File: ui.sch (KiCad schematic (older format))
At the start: 45 parts, among them SW1 SW_Push, SW2 SW_Push, SW3 SW_Push, SW4 SW_Push, SW5 SW_Push, SW8 JS202011SCQN, SW9 JS202011SCQN, U1 ICE40HX4K-TQ144

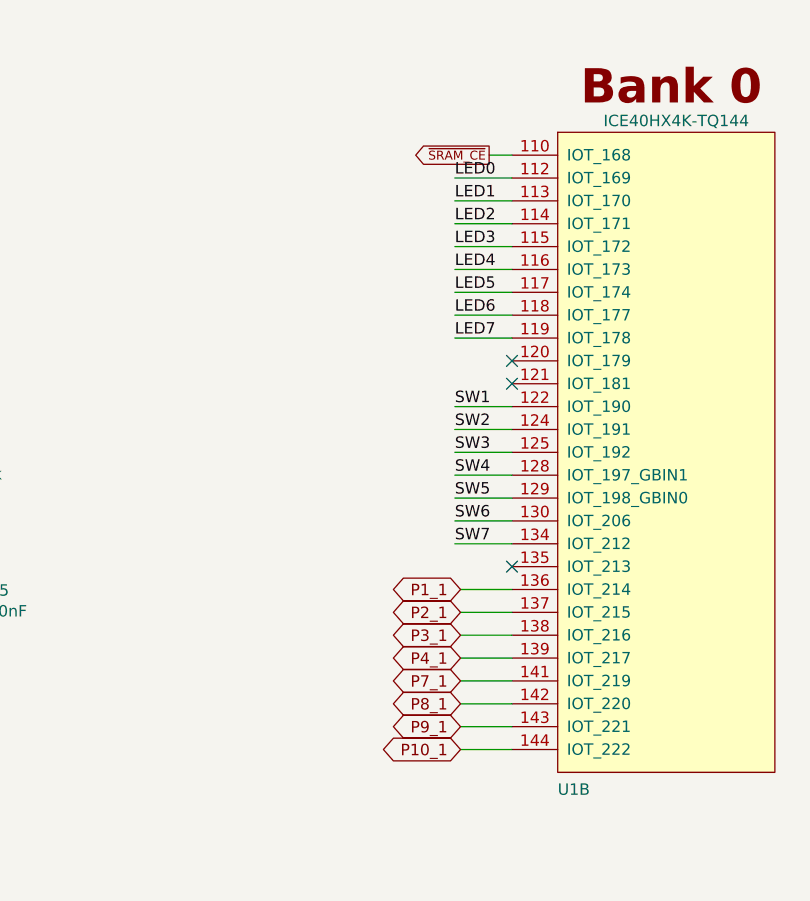
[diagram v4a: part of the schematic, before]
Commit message: Continued with routing and added ADC
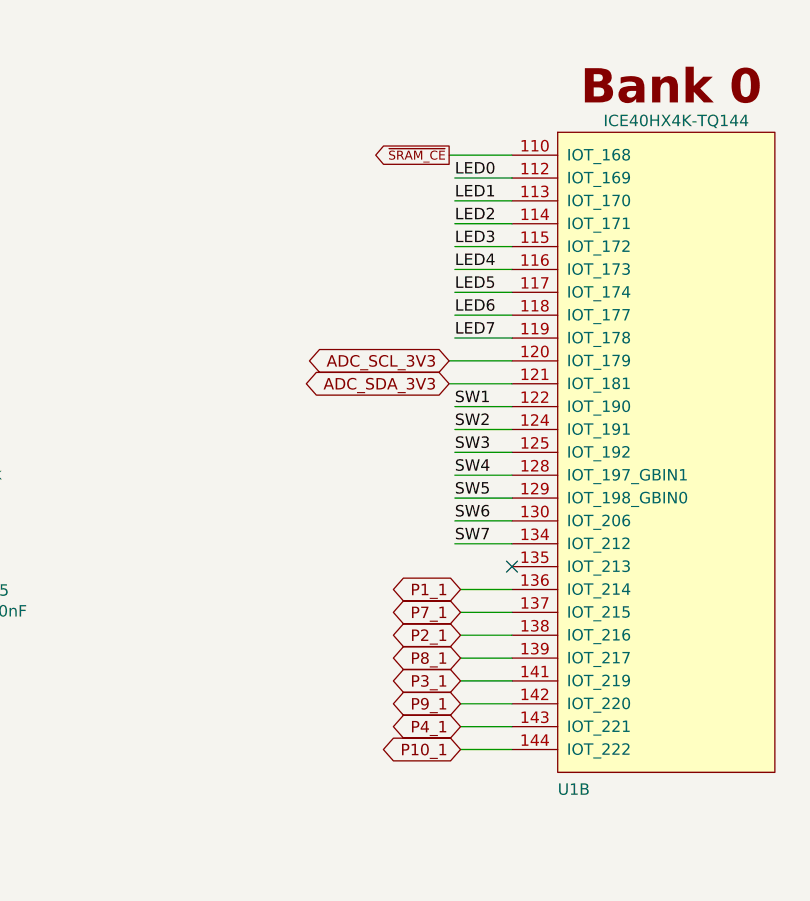
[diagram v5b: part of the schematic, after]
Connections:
- net P2_1: now also U1.138 (IOT_216); no longer U1.137 (IOT_215)
- net P3_1: now also U1.141 (IOT_219); no longer U1.138 (IOT_216)
- net P4_1: now also U1.143 (IOT_221); no longer U1.139 (IOT_217)
- net P7_1: now also U1.137 (IOT_215); no longer U1.141 (IOT_219)
- net P8_1: now also U1.139 (IOT_217); no longer U1.142 (IOT_220)
- net P9_1: now also U1.142 (IOT_220); no longer U1.143 (IOT_221)
- net ADC_SCL_3V3: now reaches U1.120 (IOT_179)
- net ADC_SDA_3V3: now reaches U1.121 (IOT_181)
- no-connect marks 11 -> 9
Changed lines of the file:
@@
 Text Label 8000 3150 0    50   ~ 0
 SW6
-Text GLabel 8025 4150 0    50   BiDi ~ 0
-P10_1
-Text GLabel 8025 4050 0    50   BiDi ~ 0
-P9_1
-Text GLabel 8025 3950 0    50   BiDi ~ 0
-P8_1
-Text GLabel 8025 3850 0    50   BiDi ~ 0
-P7_1
-Text GLabel 8025 3750 0    50   BiDi ~ 0
-P4_1
-Text GLabel 8025 3650 0    50   BiDi ~ 0
-P3_1
-Text GLabel 8025 3550 0    50   BiDi ~ 0
-P2_1
-Text GLabel 8025 3450 0    50   BiDi ~ 0
-P1_1
 Wire Wire Line
-	8025 4150 8250 4150
-Wire Wire Line
-	8025 4050 8250 4050
-Wire Wire Line
-	8025 3950 8250 3950
-Wire Wire Line
-	8025 3850 8250 3850
-Wire Wire Line
-	8025 3750 8250 3750
-Wire Wire Line
-	8025 3650 8250 3650
-Wire Wire Line
-	8025 3550 8250 3550
-Wire Wire Line
-	8025 3450 8250 3450
-Wire Wire Line
-	8150 1550 8250 1550
-Text GLabel 8150 1550 0    39   Output ~ 0
+	7975 1550 8250 1550
+Text GLabel 7975 1550 0    39   Output ~ 0
 ~SRAM_CE~
 Wire Wire Line
@@
 	1    0    0    -1
 $EndComp
-NoConn ~ 8250 2450
 NoConn ~ 8250 3350
-NoConn ~ 8250 2550
+Wire Wire Line
+	8025 3450 8250 3450
+Wire Wire Line
+	8025 3650 8250 3650
+Wire Wire Line
+	8025 3850 8250 3850
+Wire Wire Line
+	8025 4050 8250 4050
+Wire Wire Line
+	8025 3550 8250 3550
+Wire Wire Line
+	8025 3750 8250 3750
+Wire Wire Line
+	8025 3950 8250 3950
+Wire Wire Line
+	8025 4150 8250 4150
+Text GLabel 8025 3450 0    50   BiDi ~ 0
+P1_1
+Text GLabel 8025 3650 0    50   BiDi ~ 0
+P2_1
+Text GLabel 8025 3850 0    50   BiDi ~ 0
+P3_1
+Text GLabel 8025 4050 0    50   BiDi ~ 0
+P4_1
+Text GLabel 8025 3550 0    50   BiDi ~ 0
+P7_1
+Text GLabel 8025 3750 0    50   BiDi ~ 0
+P8_1
+Text GLabel 8025 3950 0    50   BiDi ~ 0
+P9_1
+Text GLabel 8025 4150 0    50   BiDi ~ 0
+P10_1
+Text GLabel 7975 2550 0    50   BiDi ~ 0
+ADC_SDA_3V3
+Text GLabel 7975 2450 0    50   BiDi ~ 0
+ADC_SCL_3V3
+Wire Wire Line
+	7975 2450 8250 2450
+Wire Wire Line
+	7975 2550 8250 2550
 $EndSCHEMATC

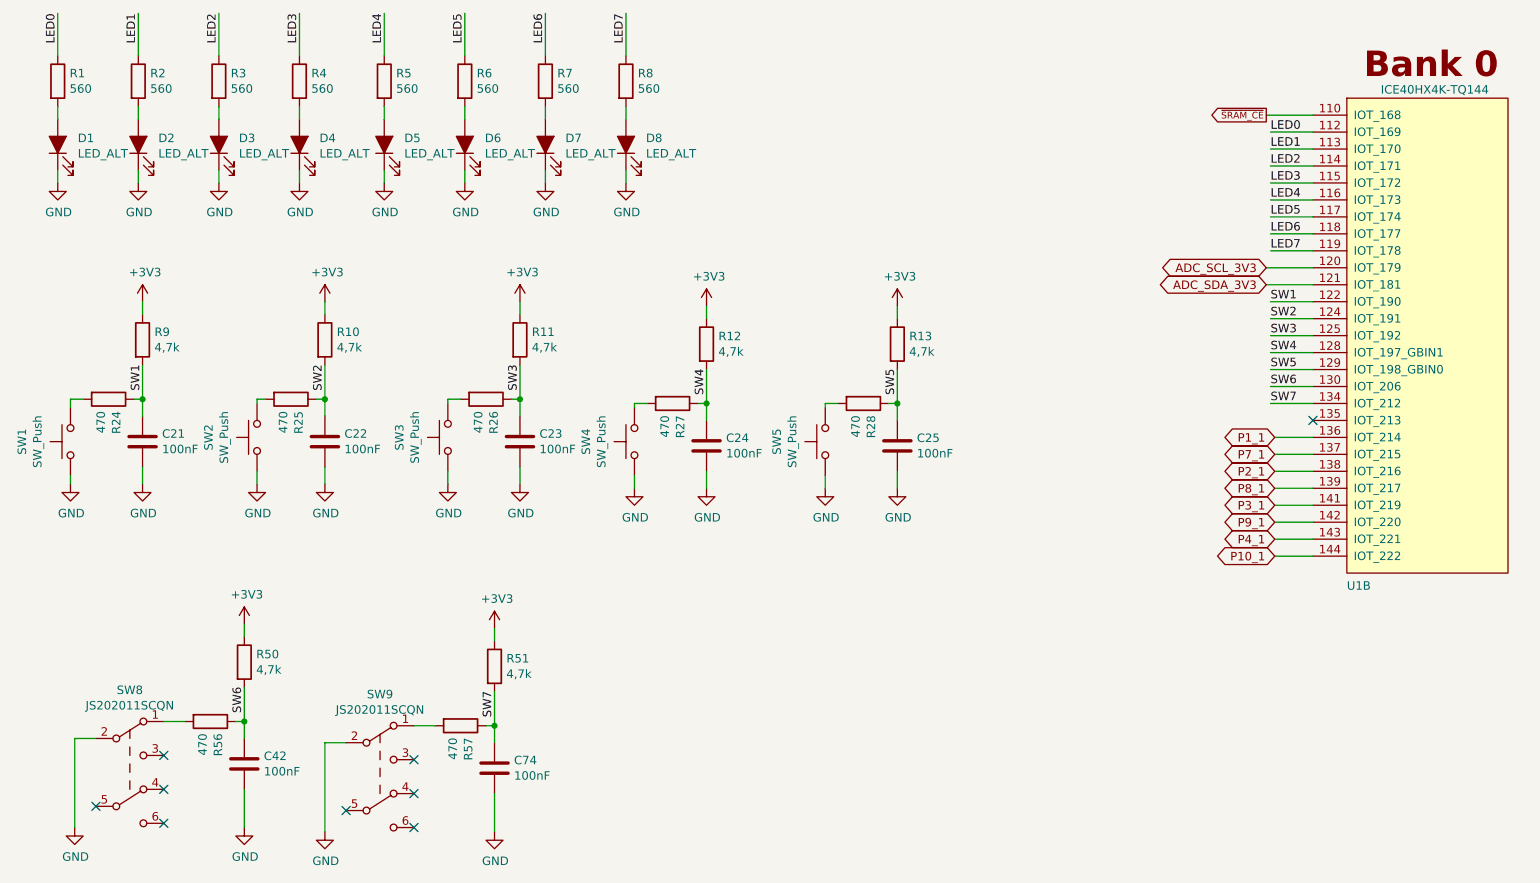
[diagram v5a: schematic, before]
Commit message: Added more BOM information, updated fpga symbol, added some more 3d models
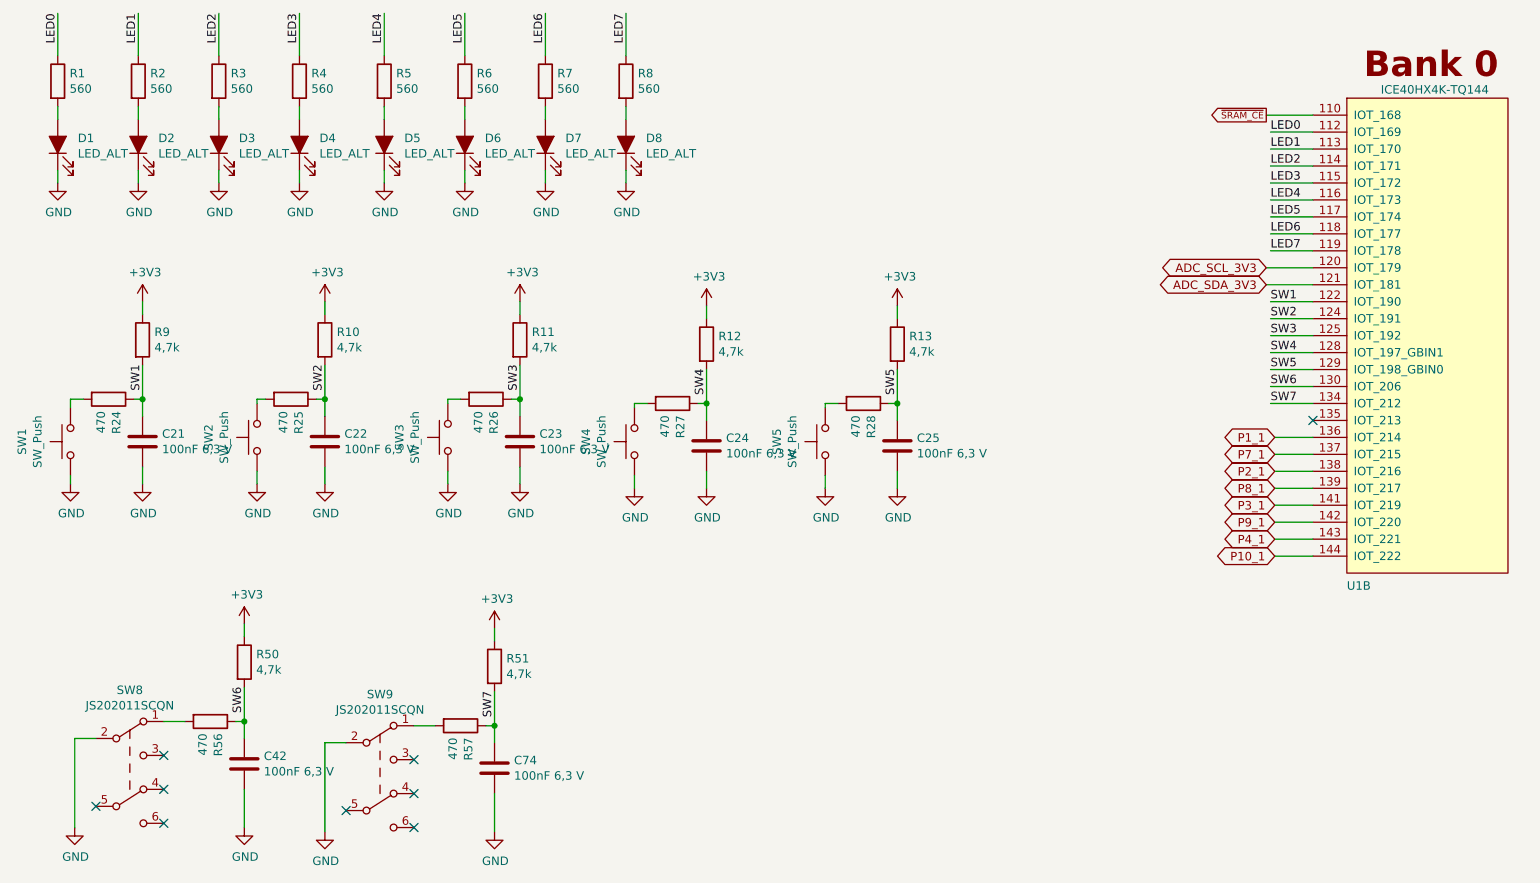
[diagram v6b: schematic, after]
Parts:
- C21, C22, C23, C24, C25, C42, C74: value 100nF -> 100nF 6,3 V; Description (none) -> CAP CER 0.1UF 50V X7R 0603; Digikey (none) -> 1276-1000-1-ND; Mfg Name (none) -> Samsung Electro-Mechanics; Mfg Part Num (none) -> CL10B104KB8NNNC; Spec (none) -> Any
- SW1, SW2, SW3, SW4, SW5, SW8, SW9: Spec (none) -> Spec
- U1: Description (none) -> IC FPGA 107 I/O 144TQFP; Digikey (none) -> 220-1572-ND; Mfg Name (none) -> Lattice Semiconductor Corporation; Mfg Part Num (none) -> ICE40HX4K-TQ144; Spec (none) -> Spec
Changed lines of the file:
@@
 F 6 "EG5350CT-ND" H 3150 3450 50  0001 C CNN "Digikey"
 F 7 "SWITCH TACTILE SPST-NO 50MA 12V" H 3150 3450 50  0001 C CNN "Description"
+F 8 "Spec" H 0   0   50  0001 C CNN "Spec"
 	1    3150 3450
 	0    -1   -1   0
@@
 F 6 "EG5350CT-ND" H 4250 3475 50  0001 C CNN "Digikey"
 F 7 "SWITCH TACTILE SPST-NO 50MA 12V" H 4250 3475 50  0001 C CNN "Description"
+F 8 "Spec" H 0   0   50  0001 C CNN "Spec"
 	1    4250 3475
 	0    -1   -1   0
@@
 F 6 "EG5350CT-ND" H 5375 3475 50  0001 C CNN "Digikey"
 F 7 "SWITCH TACTILE SPST-NO 50MA 12V" H 5375 3475 50  0001 C CNN "Description"
+F 8 "Spec" H 0   0   50  0001 C CNN "Spec"
 	1    5375 3475
 	0    -1   -1   0
@@
 P 1350 3475
 F 0 "C21" H 1465 3521 50  0000 L CNN
-F 1 "100nF" H 1465 3430 50  0000 L CNN
+F 1 "100nF 6,3 V" H 1465 3430 50  0000 L CNN
 F 2 "Capacitor_SMD:C_0603_1608Metric" H 1388 3325 50  0001 C CNN
 F 3 "~" H 1350 3475 50  0001 C CNN
+F 4 "CAP CER 0.1UF 50V X7R 0603" H 0   0   50  0001 C CNN "Description"
+F 5 "1276-1000-1-ND" H 0   0   50  0001 C CNN "Digikey"
+F 6 "Samsung Electro-Mechanics" H 0   0   50  0001 C CNN "Mfg Name"
+F 7 "CL10B104KB8NNNC" H 0   0   50  0001 C CNN "Mfg Part Num"
+F 8 "Any" H 0   0   50  0001 C CNN "Spec"
 	1    1350 3475
 	1    0    0    -1
@@
 F 6 "EG5350CT-ND" H 2025 3450 50  0001 C CNN "Digikey"
 F 7 "SWITCH TACTILE SPST-NO 50MA 12V" H 2025 3450 50  0001 C CNN "Description"
+F 8 "Spec" H 0   0   50  0001 C CNN "Spec"
 	1    2025 3450
 	0    -1   -1   0
@@
 F 6 "EG5350CT-ND" H 925 3475 50  0001 C CNN "Digikey"
 F 7 "SWITCH TACTILE SPST-NO 50MA 12V" H 925 3475 50  0001 C CNN "Description"
+F 8 "Spec" H 0   0   50  0001 C CNN "Spec"
 	1    925  3475
 	0    -1   -1   0
@@
 P 2425 3475
 F 0 "C22" H 2540 3521 50  0000 L CNN
-F 1 "100nF" H 2540 3430 50  0000 L CNN
+F 1 "100nF 6,3 V" H 2540 3430 50  0000 L CNN
 F 2 "Capacitor_SMD:C_0603_1608Metric" H 2463 3325 50  0001 C CNN
 F 3 "~" H 2425 3475 50  0001 C CNN
+F 4 "CAP CER 0.1UF 50V X7R 0603" H 0   0   50  0001 C CNN "Description"
+F 5 "1276-1000-1-ND" H 0   0   50  0001 C CNN "Digikey"
+F 6 "Samsung Electro-Mechanics" H 0   0   50  0001 C CNN "Mfg Name"
+F 7 "CL10B104KB8NNNC" H 0   0   50  0001 C CNN "Mfg Part Num"
+F 8 "Any" H 0   0   50  0001 C CNN "Spec"
 	1    2425 3475
 	1    0    0    -1
@@
 P 3575 3475
 F 0 "C23" H 3690 3521 50  0000 L CNN
-F 1 "100nF" H 3690 3430 50  0000 L CNN
+F 1 "100nF 6,3 V" H 3690 3430 50  0000 L CNN
 F 2 "Capacitor_SMD:C_0603_1608Metric" H 3613 3325 50  0001 C CNN
 F 3 "~" H 3575 3475 50  0001 C CNN
+F 4 "CAP CER 0.1UF 50V X7R 0603" H 0   0   50  0001 C CNN "Description"
+F 5 "1276-1000-1-ND" H 0   0   50  0001 C CNN "Digikey"
+F 6 "Samsung Electro-Mechanics" H 0   0   50  0001 C CNN "Mfg Name"
+F 7 "CL10B104KB8NNNC" H 0   0   50  0001 C CNN "Mfg Part Num"
+F 8 "Any" H 0   0   50  0001 C CNN "Spec"
 	1    3575 3475
 	1    0    0    -1
@@
 P 4675 3500
 F 0 "C24" H 4790 3546 50  0000 L CNN
-F 1 "100nF" H 4790 3455 50  0000 L CNN
+F 1 "100nF 6,3 V" H 4790 3455 50  0000 L CNN
 F 2 "Capacitor_SMD:C_0603_1608Metric" H 4713 3350 50  0001 C CNN
 F 3 "~" H 4675 3500 50  0001 C CNN
+F 4 "CAP CER 0.1UF 50V X7R 0603" H 0   0   50  0001 C CNN "Description"
+F 5 "1276-1000-1-ND" H 0   0   50  0001 C CNN "Digikey"
+F 6 "Samsung Electro-Mechanics" H 0   0   50  0001 C CNN "Mfg Name"
+F 7 "CL10B104KB8NNNC" H 0   0   50  0001 C CNN "Mfg Part Num"
+F 8 "Any" H 0   0   50  0001 C CNN "Spec"
 	1    4675 3500
 	1    0    0    -1
@@
 P 5800 3500
 F 0 "C25" H 5915 3546 50  0000 L CNN
-F 1 "100nF" H 5915 3455 50  0000 L CNN
+F 1 "100nF 6,3 V" H 5915 3455 50  0000 L CNN
 F 2 "Capacitor_SMD:C_0603_1608Metric" H 5838 3350 50  0001 C CNN
 F 3 "~" H 5800 3500 50  0001 C CNN
+F 4 "CAP CER 0.1UF 50V X7R 0603" H 0   0   50  0001 C CNN "Description"
+F 5 "1276-1000-1-ND" H 0   0   50  0001 C CNN "Digikey"
+F 6 "Samsung Electro-Mechanics" H 0   0   50  0001 C CNN "Mfg Name"
+F 7 "CL10B104KB8NNNC" H 0   0   50  0001 C CNN "Mfg Part Num"
+F 8 "Any" H 0   0   50  0001 C CNN "Spec"
 	1    5800 3500
 	1    0    0    -1
@@
 F 6 "401-2002-1-ND" H 1275 5425 50  0001 C CNN "Digikey"
 F 7 "SWITCH SLIDE DPDT 300MA 6V" H 1275 5425 50  0001 C CNN "Description"
+F 8 "Spec" H 0   0   50  0001 C CNN "Spec"
 	1    1275 5425
 	1    0    0    -1
@@
 P 1950 5375
 F 0 "C42" H 2065 5421 50  0000 L CNN
-F 1 "100nF" H 2065 5330 50  0000 L CNN
+F 1 "100nF 6,3 V" H 2065 5330 50  0000 L CNN
 F 2 "Capacitor_SMD:C_0603_1608Metric" H 1988 5225 50  0001 C CNN
 F 3 "~" H 1950 5375 50  0001 C CNN
+F 4 "CAP CER 0.1UF 50V X7R 0603" H 0   0   50  0001 C CNN "Description"
+F 5 "1276-1000-1-ND" H 0   0   50  0001 C CNN "Digikey"
+F 6 "Samsung Electro-Mechanics" H 0   0   50  0001 C CNN "Mfg Name"
+F 7 "CL10B104KB8NNNC" H 0   0   50  0001 C CNN "Mfg Part Num"
+F 8 "Any" H 0   0   50  0001 C CNN "Spec"
 	1    1950 5375
 	1    0    0    -1
@@
 F 6 "401-2002-1-ND" H 2750 5450 50  0001 C CNN "Digikey"
 F 7 "SWITCH SLIDE DPDT 300MA 6V" H 2750 5450 50  0001 C CNN "Description"
+F 8 "Spec" H 0   0   50  0001 C CNN "Spec"
 	1    2750 5450
 	1    0    0    -1
@@
 P 3425 5400
 F 0 "C74" H 3540 5446 50  0000 L CNN
-F 1 "100nF" H 3540 5355 50  0000 L CNN
+F 1 "100nF 6,3 V" H 3540 5355 50  0000 L CNN
 F 2 "Capacitor_SMD:C_0603_1608Metric" H 3463 5250 50  0001 C CNN
 F 3 "~" H 3425 5400 50  0001 C CNN
+F 4 "CAP CER 0.1UF 50V X7R 0603" H 0   0   50  0001 C CNN "Description"
+F 5 "1276-1000-1-ND" H 0   0   50  0001 C CNN "Digikey"
+F 6 "Samsung Electro-Mechanics" H 0   0   50  0001 C CNN "Mfg Name"
+F 7 "CL10B104KB8NNNC" H 0   0   50  0001 C CNN "Mfg Part Num"
+F 8 "Any" H 0   0   50  0001 C CNN "Spec"
 	1    3425 5400
 	1    0    0    -1
@@
 U 2 1 5CAB837C
 P 8450 2850
+AR Path="/5CAB837C" Ref="U1"  Part="2"
+AR Path="/5CAB7CD4/5CAB837C" Ref="U1"  Part="2"
 F 0 "U1" H 8450 1375 50  0000 L CNN
 F 1 "ICE40HX4K-TQ144" H 8650 4300 50  0000 L CNN
 F 2 "" H 8450 2850 50  0001 C CNN
 F 3 "" H 8450 2850 50  0001 C CNN
+F 4 "IC FPGA 107 I/O 144TQFP" H 0   0   50  0001 C CNN "Description"
+F 5 "220-1572-ND" H 0   0   50  0001 C CNN "Digikey"
+F 6 "Lattice Semiconductor Corporation" H 0   0   50  0001 C CNN "Mfg Name"
+F 7 "ICE40HX4K-TQ144" H 0   0   50  0001 C CNN "Mfg Part Num"
+F 8 "Spec" H 0   0   50  0001 C CNN "Spec"
 	2    8450 2850
 	1    0    0    -1
